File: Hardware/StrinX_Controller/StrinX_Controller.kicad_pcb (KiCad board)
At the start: 2 copper layers, 42 parts, among them J1 HWB, J10 ENC, J2 USB_C_16p, J3 I2C, J4 JoyA, J5 JoyB, J6 SW1, J7 SW2, J8 SW3, J9 SW4, SW1 RST, U1 ATmega32U4-A, U2 AMS1117-3.3, U3 NRF24L01, Y1 16MHz

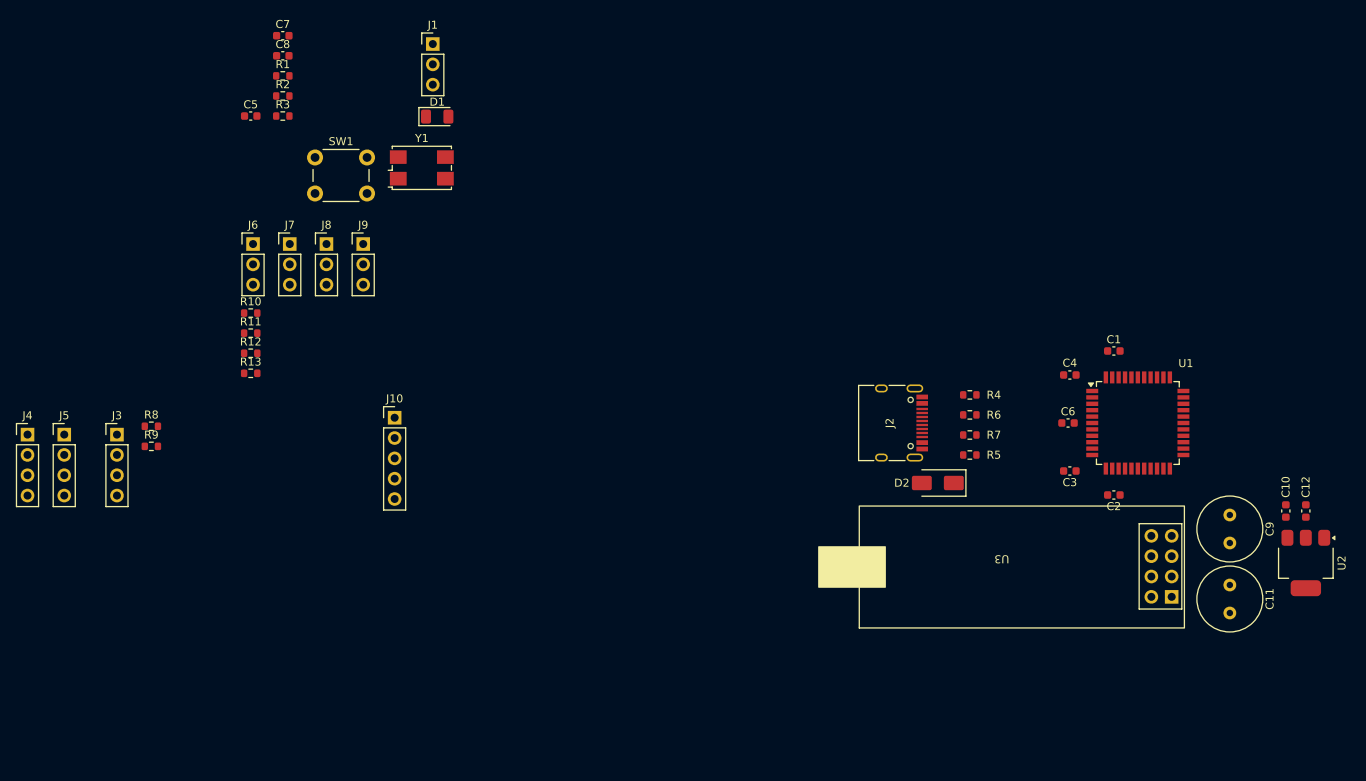
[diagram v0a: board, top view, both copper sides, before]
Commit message: Update some device connection and Complete PCB
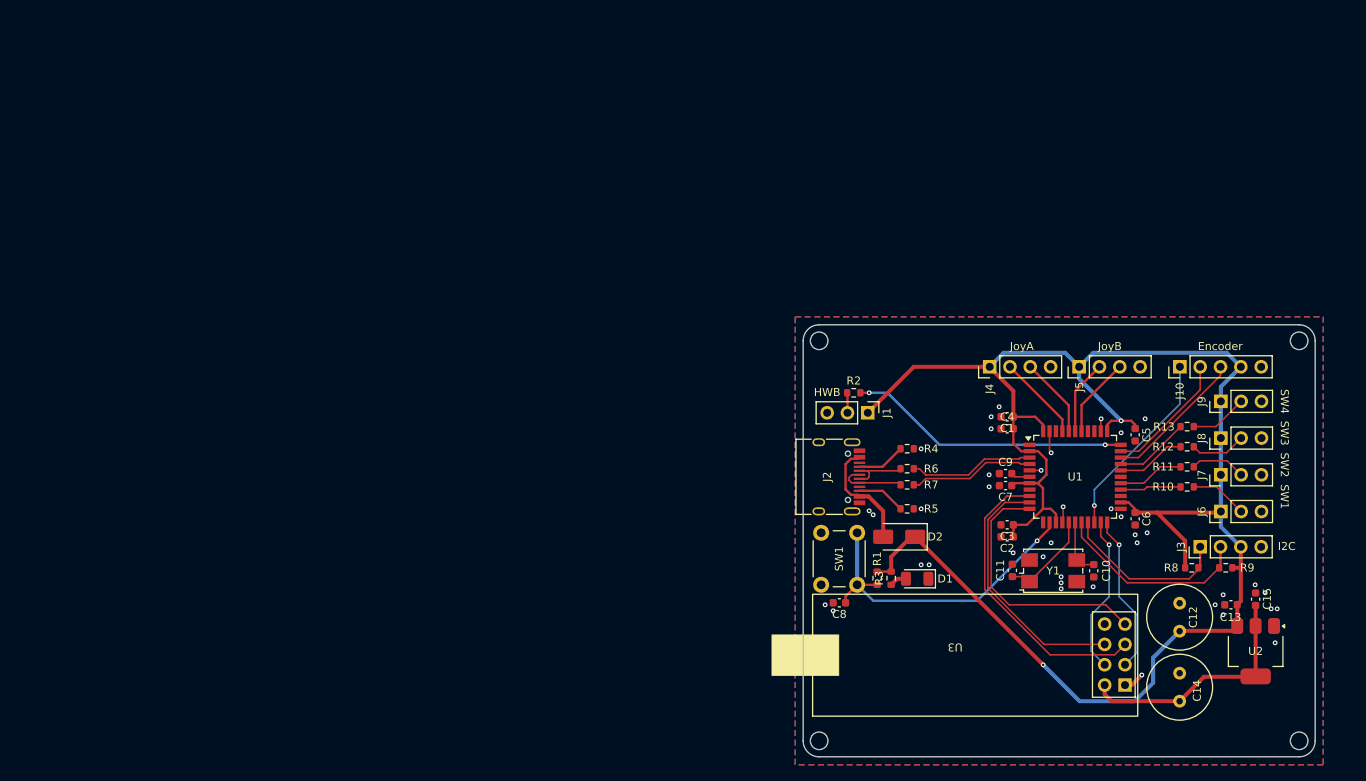
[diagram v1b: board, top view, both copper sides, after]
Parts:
- added C5: 100n, Capacitor_SMD:C_0603_1608Metric, F.Cu at (159.7, 91.5)
- added C6: 100n, Capacitor_SMD:C_0603_1608Metric, F.Cu at (159.7, 102.0)
- added C7: 100n, Capacitor_SMD:C_0603_1608Metric, F.Cu at (143.5, 97.8)
- added REF**: MountingHole_2.2mm_M2_ISO7380, MountingHole:MountingHole_2.2mm_M2_ISO7380, F.Cu at (180.2, 129.7)
- added REF**: MountingHole_2.2mm_M2_ISO7380, MountingHole:MountingHole_2.2mm_M2_ISO7380, F.Cu at (120.2, 79.7)
- added REF**: MountingHole_2.2mm_M2_ISO7380, MountingHole:MountingHole_2.2mm_M2_ISO7380, F.Cu at (120.2, 129.7)
- added REF**: MountingHole_2.2mm_M2_ISO7380, MountingHole:MountingHole_2.2mm_M2_ISO7380, F.Cu at (180.2, 79.7)
- moved J3 136.1 mm to (167.8, 105.5), turned to 90 degrees
- moved R9 135.2 mm to (171.0, 108.1), turned to 180 degrees
- moved R8 131.2 mm to (166.7, 108.1)
- moved J5 127.1 mm to (152.7, 83.0), turned to 90 degrees
- moved J6 125.5 mm to (170.4, 101.1), turned to 90 degrees
- moved C10 121.4 mm to (154.5, 108.5), turned to 90 degrees
- moved J4 120.6 mm to (141.5, 83.0), turned to 90 degrees
- moved J7 119.9 mm to (170.4, 96.5), turned to 90 degrees
- moved R10 119.1 mm to (166.2, 98.0)
- moved R11 118.2 mm to (166.2, 95.5)
- moved R12 117.6 mm to (166.2, 93.0)
- moved R13 117.2 mm to (166.2, 90.5)
- moved J8 114.4 mm to (170.4, 91.9), turned to 90 degrees
- moved C11 111.6 mm to (144.3, 108.4), turned to -90 degrees
- moved J9 109.0 mm to (170.4, 87.3), turned to 90 degrees
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- renumbered C7 to C10, C8 to C11, C9 to C12, C10 to C13, C11 to C14, C12 to C15, C5 to C8, C6 to C9
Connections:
- U1 pad 20: /AT32u4/SW1 -> /AT32u4/CK
- U1 pad 21: /AT32u4/SW2 -> /AT32u4/~{CSN}
- U1 pad 22: /AT32u4/SW4 -> /AT32u4/CE
- U1 pad 25: /AT32u4/SW3 -> unconnected-(U1-PD4-Pad25)
- U1 pad 26: /AT32u4/~{CSN} -> /AT32u4/SW1
- U1 pad 27: /AT32u4/CE -> /AT32u4/SW2
- U1 pad 28: /AT32u4/CK -> unconnected-(U1-PB4-Pad28)
- U1 pad 29: /AT32u4/DT -> /AT32u4/SW3
- U1 pad 30: unconnected-(U1-PB6-Pad30) -> /AT32u4/SW4
- U1 pad 31: unconnected-(U1-PC6-Pad31) -> /AT32u4/BTN
- U1 pad 32: /AT32u4/BTN -> /AT32u4/DT
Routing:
- net +5V: track 0.00 -> 225.6 mm, vias 0 -> 2
- net /AT32u4/RST: track 0.00 -> 41.2 mm, vias 0 -> 1
- net /AT32u4/SCK: track 0.00 -> 37.1 mm
- net /AT32u4/HWB: track 0.00 -> 35.2 mm, vias 0 -> 2
- net /AT32u4/MISO: track 0.00 -> 32.3 mm
- net /AT32u4/MOSI: track 0.00 -> 32.2 mm
- net +3V3: track 0.00 -> 30.5 mm
- net /AT32u4/SCL: track 0.00 -> 24.9 mm
- net /AT32u4/CK: track 0.00 -> 23.9 mm, vias 0 -> 1
- net /AT32u4/SDA: track 0.00 -> 21.3 mm
- net /AT32u4/CE: track 0.00 -> 20.0 mm, vias 0 -> 1
- net /AT32u4/~{CSN}: track 0.00 -> 19.9 mm, vias 0 -> 1
- net /AT32u4/BTN: track 0.00 -> 17.8 mm
- net /AT32u4/DT: track 0.00 -> 16.0 mm
- net /AT32u4/D-: track 0.00 -> 15.7 mm
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- added copper zone on B.Cu, net GND
- added copper zone on F.Cu, net GND
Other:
- board outline added: 64 x 54 mm
- board text added: "Designed by KappyPhm"
- board text added: "Encoder"
- board text added: "HWB"
- board text added: "I2C"
- board text added: "JoyA"
- board text added: "JoyB"
- board text added: "STRIX CONTROLLER"
- board text added: "SW4 SW3 SW2 SW1"
